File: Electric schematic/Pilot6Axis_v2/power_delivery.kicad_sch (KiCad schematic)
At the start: 45 parts, among them IC2 TPS25751SRSMR, IC3 BQ25792RQMR, Q3 AO3400A, Q4 AO3400A

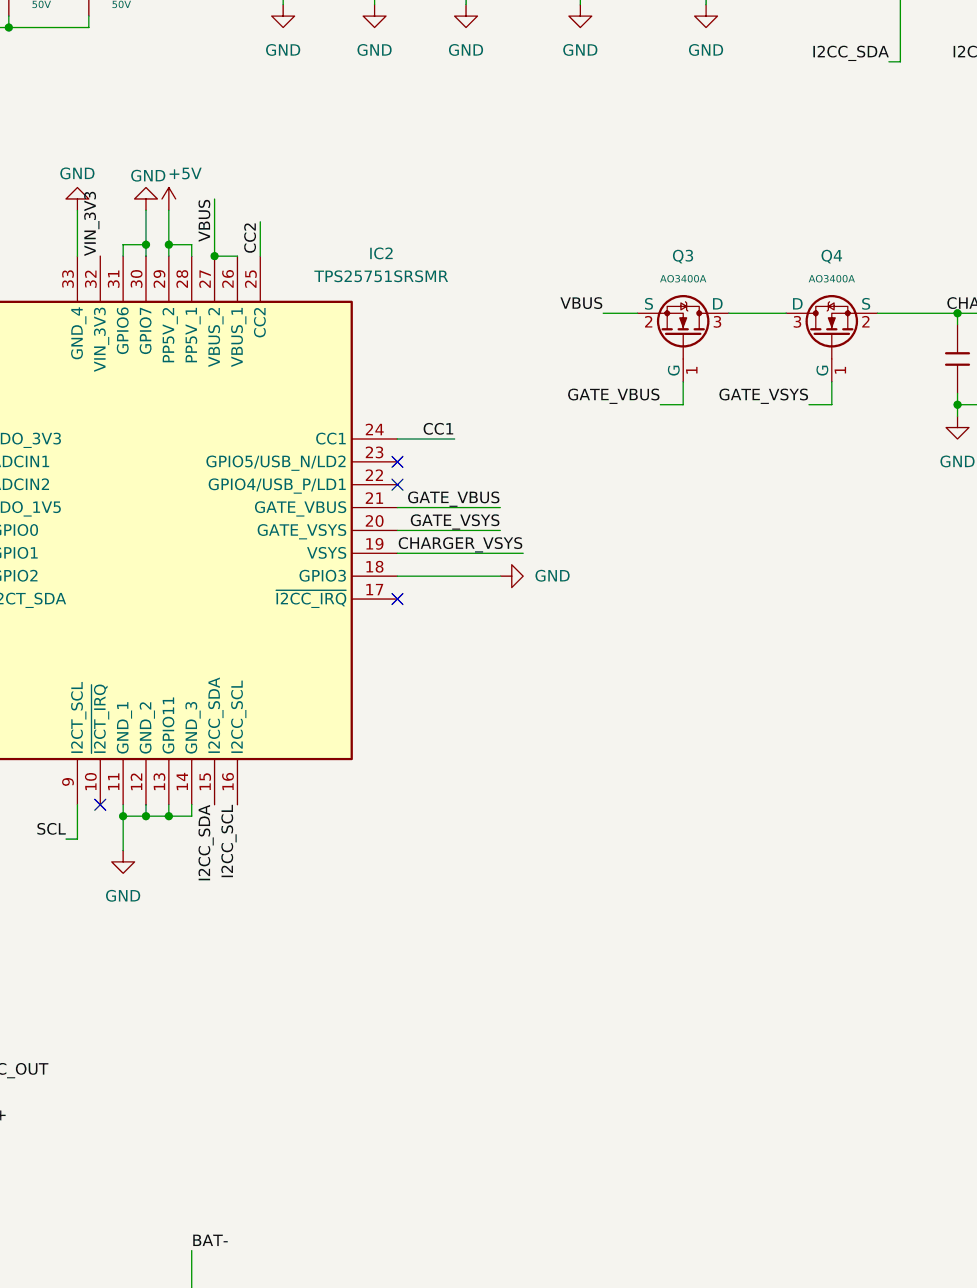
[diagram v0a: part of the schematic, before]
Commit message: [pcb] added eeprom to pd charger so the ciofnig is remembered and set correctly
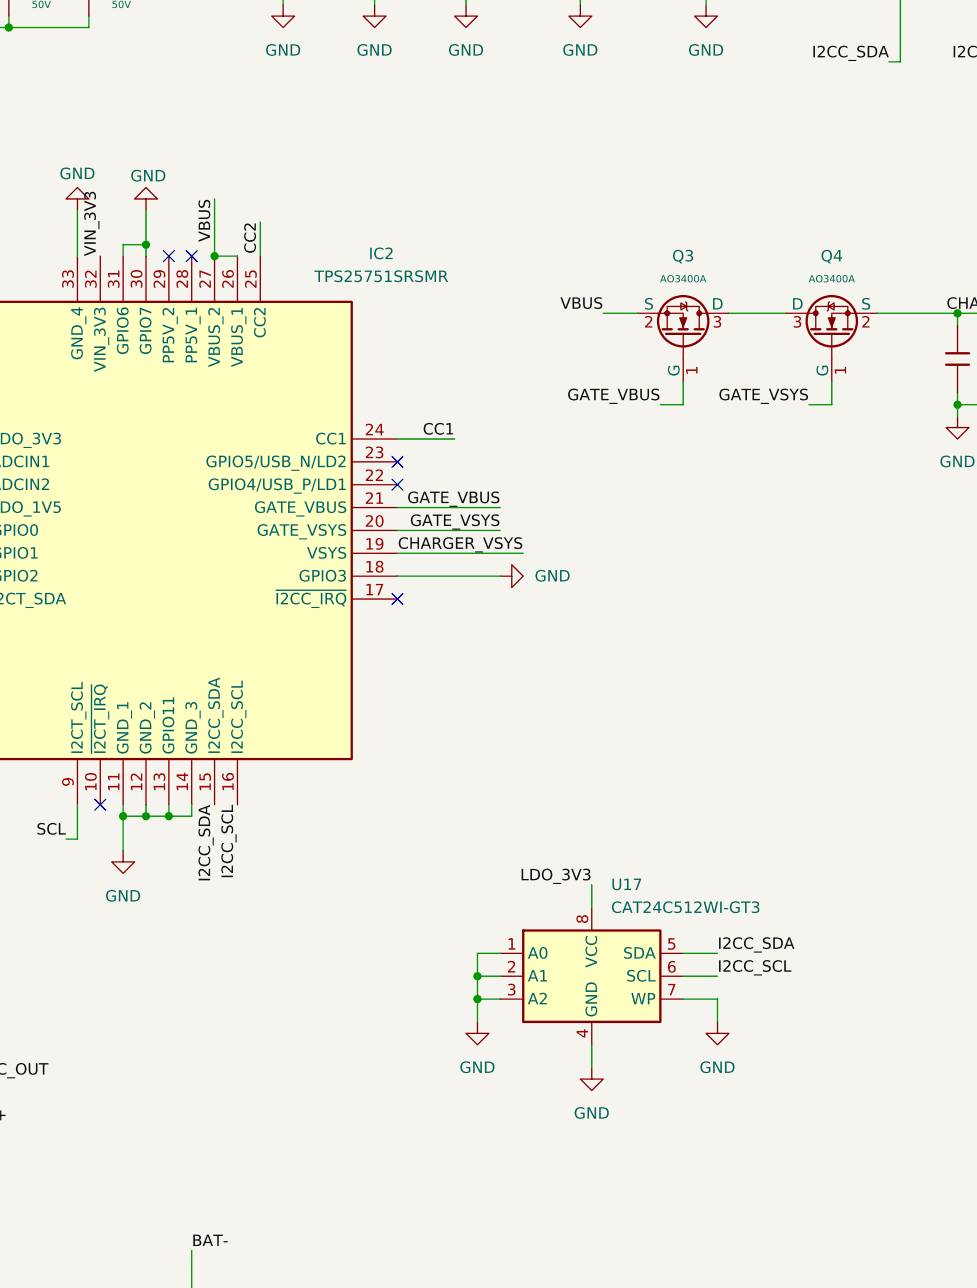
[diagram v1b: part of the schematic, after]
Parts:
- added U17: CAT24C512WI-GT3, Package_SO:SOIC-8_3.9x4.9mm_P1.27mm, symbol Memory_EEPROM:AT24CS02-SSHM
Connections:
- net GND: now also U17.1 (A0), U17.2 (A1), U17.3 (A2), U17.4 (GND), U17.7 (WP)
- net I2CC_SCL: now also U17.6 (SCL)
- net I2CC_SDA: now also U17.5 (SDA)
- net LDO_3V3: now also U17.8 (VCC)
- net +5V: no longer names the net of IC2.28 (PP5V_1)
- net +5V: no longer IC2.29 (PP5V_2)
- no-connect marks 9 -> 11
